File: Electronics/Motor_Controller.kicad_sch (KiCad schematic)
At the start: 43 parts, among them J2 SWCLK SWD, SW1 SW_Push, SW2 ~{USB_BOOT}, U1 RP2040, U4 W25Q32JVZP, Y1 ABM8-272-T3

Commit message: power + usb
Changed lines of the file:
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@@
     (effects (font (size 1.27 1.27)) (justify left))
   )
-  (hierarchical_label "USB+" (shape input) (at 44.45 49.53 180) (fields_autoplaced)
+  (hierarchical_label "USB+" (shape bidirectional) (at 44.45 49.53 180) (fields_autoplaced)
     (effects (font (size 1.27 1.27)) (justify right))
   )
-  (hierarchical_label "USB-" (shape input) (at 44.45 52.07 180) (fields_autoplaced)
+  (hierarchical_label "USB-" (shape bidirectional) (at 44.45 52.07 180) (fields_autoplaced)
     (effects (font (size 1.27 1.27)) (justify right))
   )

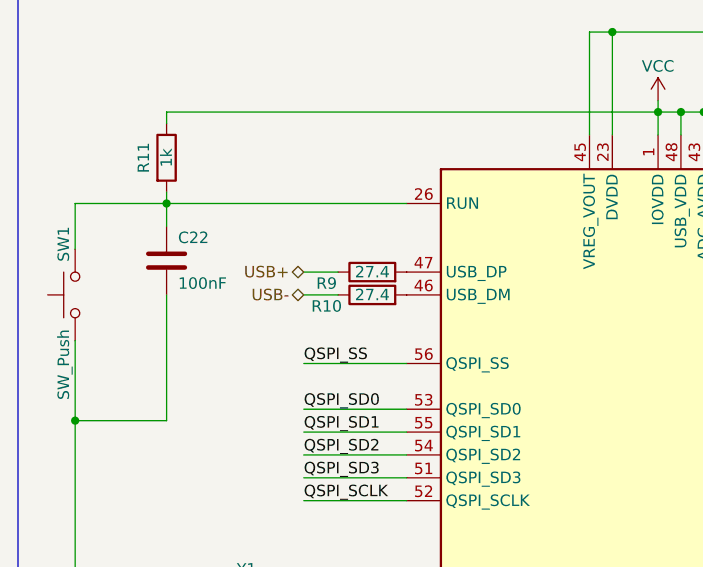
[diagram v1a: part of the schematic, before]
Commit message: USB to UART converter
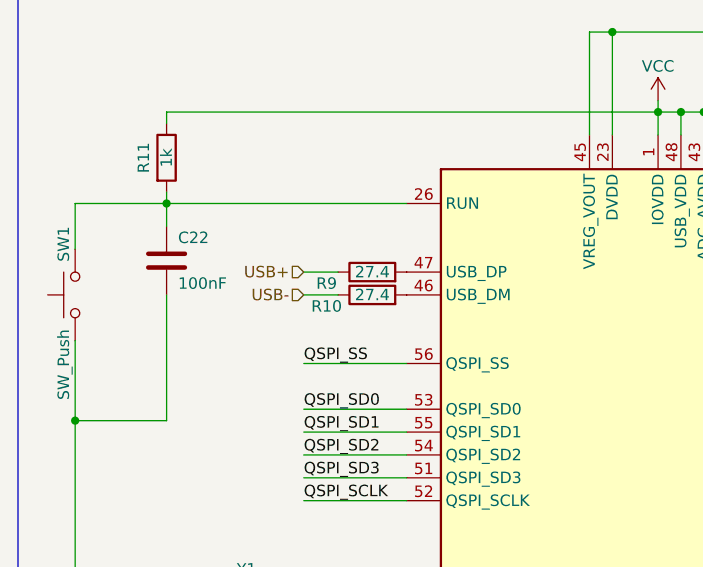
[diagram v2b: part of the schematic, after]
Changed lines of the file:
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@@
     (effects (font (size 1.27 1.27)) (justify left))
   )
-  (hierarchical_label "USB+" (shape bidirectional) (at 44.45 49.53 180) (fields_autoplaced)
+  (hierarchical_label "USB+" (shape input) (at 44.45 49.53 180) (fields_autoplaced)
     (effects (font (size 1.27 1.27)) (justify right))
   )
-  (hierarchical_label "USB-" (shape bidirectional) (at 44.45 52.07 180) (fields_autoplaced)
+  (hierarchical_label "USB-" (shape input) (at 44.45 52.07 180) (fields_autoplaced)
     (effects (font (size 1.27 1.27)) (justify right))
   )
